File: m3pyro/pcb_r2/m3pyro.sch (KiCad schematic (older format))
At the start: 67 parts, among them IC1 STM32F405RxTx, IC2 TPS62130, IC3 MCP2562, IC4 TPS62150, J1 WEST TOP, J2 WEST BOT, J3 EAST TOP, J4 EAST BOT, Q1 Si5515CDC, Q2 Si5515CDC, Q3 Si5515CDC, Q4 Si5515CDC, Q5 Si5515CDC, Q6 Si5515CDC, Q7 Si5515CDC, Q8 Si5515CDC, Y1 26M

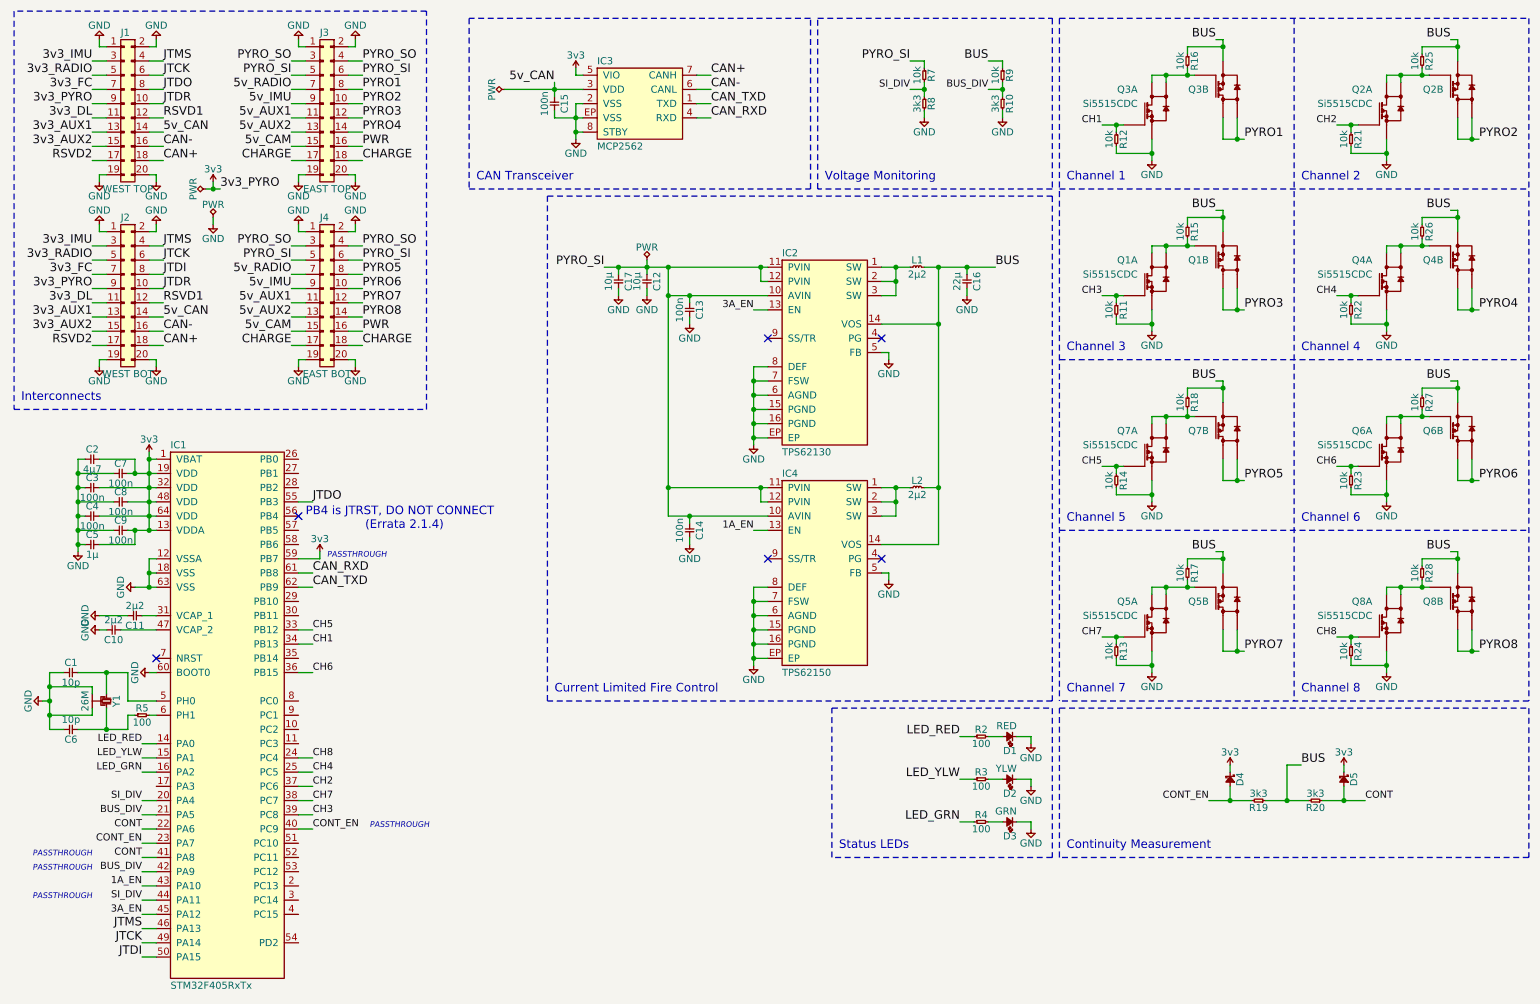
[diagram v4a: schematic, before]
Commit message: Update m3pyro so ch1-4 are bottom, 5-8 are top
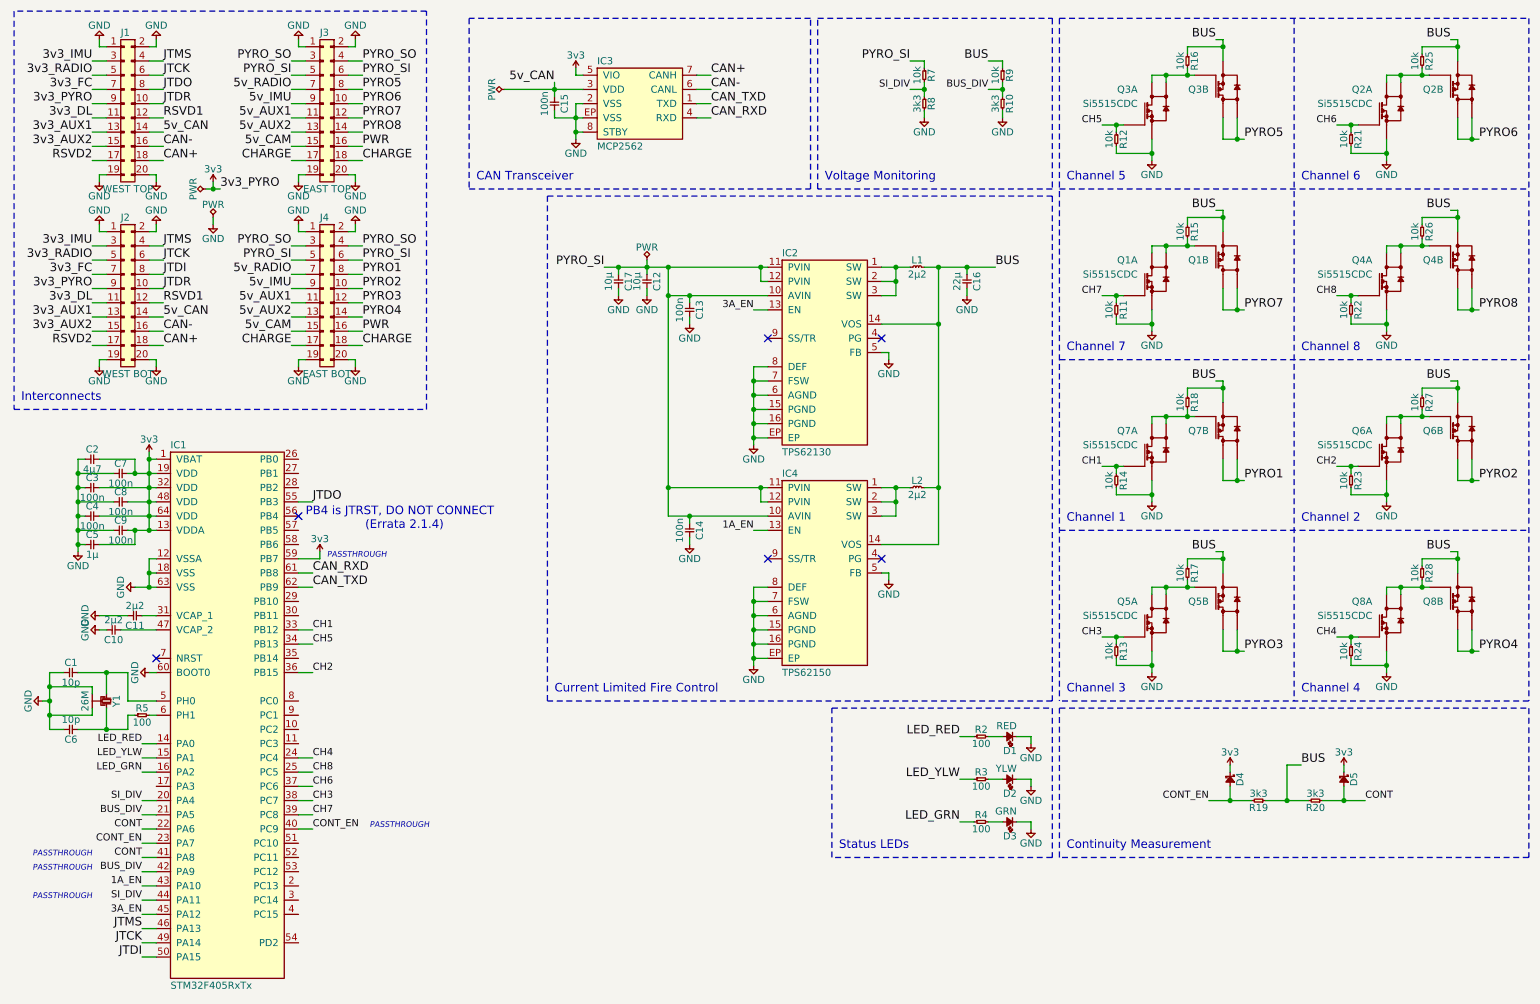
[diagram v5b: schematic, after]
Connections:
- net CH1: now also IC1.33 (PB12), Q7.2 (G1), R14.1; no longer IC1.34 (PB13), Q3.2 (G1), R12.1
- net CH2: now also IC1.36 (PB15), Q6.2 (G1), R23.1; no longer IC1.37 (PC6), Q2.2 (G1), R21.1
- net CH3: now also IC1.38 (PC7), Q5.2 (G1), R13.1; no longer IC1.39 (PC8), Q1.2 (G1), R11.1
- net CH4: now also IC1.24 (PC4), Q8.2 (G1), R24.1; no longer IC1.25 (PC5), Q4.2 (G1), R22.1
- net CH5: now also IC1.34 (PB13), Q3.2 (G1), R12.1; no longer IC1.33 (PB12), Q7.2 (G1), R14.1
- net CH6: now also IC1.37 (PC6), Q2.2 (G1), R21.1; no longer IC1.36 (PB15), Q6.2 (G1), R23.1
- net CH7: now also IC1.39 (PC8), Q1.2 (G1), R11.1; no longer IC1.38 (PC7), Q5.2 (G1), R13.1
- net CH8: now also IC1.25 (PC5), Q4.2 (G1), R22.1; no longer IC1.24 (PC4), Q8.2 (G1), R24.1
- net PYRO1: now also J4.8, Q7.5 (D2), Q7.6 (D2); no longer J3.8, Q3.5 (D2), Q3.6 (D2)
- net PYRO2: now also J4.10, Q6.5 (D2), Q6.6 (D2); no longer J3.10, Q2.5 (D2), Q2.6 (D2)
- net PYRO3: now also J4.12, Q5.5 (D2), Q5.6 (D2); no longer J3.12, Q1.5 (D2), Q1.6 (D2)
- net PYRO4: now also J4.14, Q8.5 (D2), Q8.6 (D2); no longer J3.14, Q4.5 (D2), Q4.6 (D2)
- net PYRO5: now also J3.8, Q3.5 (D2), Q3.6 (D2); no longer J4.8, Q7.5 (D2), Q7.6 (D2)
- net PYRO6: now also J3.10, Q2.5 (D2), Q2.6 (D2); no longer J4.10, Q6.5 (D2), Q6.6 (D2)
- net PYRO7: now also J3.12, Q1.5 (D2), Q1.6 (D2); no longer J4.12, Q5.5 (D2), Q5.6 (D2)
- net PYRO8: now also J3.14, Q4.5 (D2), Q4.6 (D2); no longer J4.14, Q8.5 (D2), Q8.6 (D2)
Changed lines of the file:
@@
 Text Label 2950 1450 0    60   ~ 0
 PWR
-Text Label 2950 1350 0    60   ~ 0
+Text Label 2950 2650 0    60   ~ 0
 PYRO4
-Text Label 2950 1250 0    60   ~ 0
+Text Label 2950 2550 0    60   ~ 0
 PYRO3
-Text Label 2950 1150 0    60   ~ 0
+Text Label 2950 2450 0    60   ~ 0
 PYRO2
-Text Label 2950 1050 0    60   ~ 0
+Text Label 2950 2350 0    60   ~ 0
 PYRO1
 $Comp
@@
 Text Label 2950 2750 0    60   ~ 0
 PWR
-Text Label 2950 2650 0    60   ~ 0
+Text Label 2950 1350 0    60   ~ 0
 PYRO8
-Text Label 2950 2550 0    60   ~ 0
+Text Label 2950 1250 0    60   ~ 0
 PYRO7
-Text Label 2950 2450 0    60   ~ 0
+Text Label 2950 1150 0    60   ~ 0
 PYRO6
-Text Label 2950 2350 0    60   ~ 0
+Text Label 2950 1050 0    60   ~ 0
 PYRO5
 Text Notes 550  3250 0    60   ~ 0
@@
 	2950 1450 2850 1450
 Wire Wire Line
+	2850 2650 2950 2650
+Wire Wire Line
+	2850 2550 2950 2550
+Wire Wire Line
+	2950 2450 2850 2450
+Wire Wire Line
+	2850 2350 2950 2350
+Wire Wire Line
+	2950 950  2850 950
+Wire Wire Line
+	2850 850  2950 850
+Wire Wire Line
+	2850 2050 2900 2050
+Wire Wire Line
+	2900 2050 2900 2000
+Wire Wire Line
+	2550 2050 2500 2050
+Wire Wire Line
+	2500 2050 2500 2000
+Wire Wire Line
+	2550 2950 2500 2950
+Wire Wire Line
+	2500 2950 2500 3000
+Wire Wire Line
+	2850 2950 2900 2950
+Wire Wire Line
+	2900 2950 2900 3000
+Wire Wire Line
+	2550 2150 2450 2150
+Wire Wire Line
+	2450 2250 2550 2250
+Wire Wire Line
+	2550 2350 2450 2350
+Wire Wire Line
+	2450 2450 2550 2450
+Wire Wire Line
+	2550 2550 2450 2550
+Wire Wire Line
+	2450 2650 2550 2650
+Wire Wire Line
+	2550 2750 2450 2750
+Wire Wire Line
+	2450 2850 2550 2850
+Wire Wire Line
+	2850 2850 2950 2850
+Wire Wire Line
+	2950 2750 2850 2750
+Wire Wire Line
 	2850 1350 2950 1350
 Wire Wire Line
@@
 Wire Wire Line
 	2850 1050 2950 1050
-Wire Wire Line
-	2950 950  2850 950
-Wire Wire Line
-	2850 850  2950 850
-Wire Wire Line
-	2850 2050 2900 2050
-Wire Wire Line
-	2900 2050 2900 2000
-Wire Wire Line
-	2550 2050 2500 2050
-Wire Wire Line
-	2500 2050 2500 2000
-Wire Wire Line
-	2550 2950 2500 2950
-Wire Wire Line
-	2500 2950 2500 3000
-Wire Wire Line
-	2850 2950 2900 2950
-Wire Wire Line
-	2900 2950 2900 3000
-Wire Wire Line
-	2550 2150 2450 2150
-Wire Wire Line
-	2450 2250 2550 2250
-Wire Wire Line
-	2550 2350 2450 2350
-Wire Wire Line
-	2450 2450 2550 2450
-Wire Wire Line
-	2550 2550 2450 2550
-Wire Wire Line
-	2450 2650 2550 2650
-Wire Wire Line
-	2550 2750 2450 2750
-Wire Wire Line
-	2450 2850 2550 2850
-Wire Wire Line
-	2850 2850 2950 2850
-Wire Wire Line
-	2950 2750 2850 2750
-Wire Wire Line
-	2850 2650 2950 2650
-Wire Wire Line
-	2850 2550 2950 2550
-Wire Wire Line
-	2950 2450 2850 2450
-Wire Wire Line
-	2850 2350 2950 2350
 Wire Wire Line
 	2950 2250 2850 2250
@@
 Connection ~ 8250 1300
 Text Label 8150 1300 2    50   ~ 0
-CH1
+CH5
 Wire Wire Line
 	8500 1000 8500 950
@@
 	9000 1400 9150 1400
 Text Label 9150 1400 0    60   ~ 0
-PYRO1
+PYRO5
 Wire Wire Line
 	8500 950  8800 950
@@
 	7850 550  7850 5350
 Text Notes 7900 1700 0    60   ~ 0
-Channel 1
+Channel 5
 Wire Notes Line
 	7850 550  11150 550
@@
 Connection ~ 9900 1300
 Text Label 9800 1300 2    50   ~ 0
-CH2
+CH6
 Wire Wire Line
 	10150 1000 10150 950
@@
 	10650 1400 10800 1400
 Text Label 10800 1400 0    60   ~ 0
-PYRO2
+PYRO6
 Wire Wire Line
 	10150 950  10450 950
@@
 	9500 550  9500 5350
 Text Notes 9550 1700 0    60   ~ 0
-Channel 2
+Channel 6
 $Comp
 L Si5515CDC Q1
@@
 Connection ~ 8250 2500
 Text Label 8150 2500 2    50   ~ 0
-CH3
+CH7
 Wire Wire Line
 	8500 2200 8500 2150
@@
 	9000 2600 9150 2600
 Text Label 9150 2600 0    60   ~ 0
-PYRO3
+PYRO7
 Wire Wire Line
 	8500 2150 8800 2150
@@
 Connection ~ 9100 2600
 Text Notes 7900 2900 0    60   ~ 0
-Channel 3
+Channel 7
 Wire Notes Line
 	7850 1750 11150 1750
@@
 Connection ~ 9900 2500
 Text Label 9800 2500 2    50   ~ 0
-CH4
+CH8
 Wire Wire Line
 	10150 2200 10150 2150
@@
 	10650 2600 10800 2600
 Text Label 10800 2600 0    60   ~ 0
-PYRO4
+PYRO8
 Wire Wire Line
 	10150 2150 10450 2150
@@
 Connection ~ 10750 2600
 Text Notes 9550 2900 0    60   ~ 0
-Channel 4
+Channel 8
 $Comp
 L Si5515CDC Q7
@@
 Connection ~ 8250 3700
 Text Label 8150 3700 2    50   ~ 0
-CH5
+CH1
 Wire Wire Line
 	8500 3400 8500 3350
@@
 	9000 3800 9150 3800
 Text Label 9150 3800 0    60   ~ 0
-PYRO5
+PYRO1
 Wire Wire Line
 	8500 3350 8800 3350
@@
 Connection ~ 9100 3800
 Text Notes 7900 4100 0    60   ~ 0
-Channel 5
+Channel 1
 Wire Notes Line
 	7850 2950 11150 2950
@@
 Connection ~ 9900 3700
 Text Label 9800 3700 2    50   ~ 0
-CH6
+CH2
 Wire Wire Line
 	10150 3400 10150 3350
@@
 	10650 3800 10800 3800
 Text Label 10800 3800 0    60   ~ 0
-PYRO6
+PYRO2
 Wire Wire Line
 	10150 3350 10450 3350
@@
 Connection ~ 10750 3800
 Text Notes 9550 4100 0    60   ~ 0
-Channel 6
+Channel 2
 $Comp
 L Si5515CDC Q5
@@
 Connection ~ 8250 4900
 Text Label 8150 4900 2    50   ~ 0
-CH7
+CH3
 Wire Wire Line
 	8500 4600 8500 4550
@@
 	9000 5000 9150 5000
 Text Label 9150 5000 0    60   ~ 0
-PYRO7
+PYRO3
 Wire Wire Line
 	8500 4550 8800 4550
@@
 Connection ~ 9100 5000
 Text Notes 7900 5300 0    60   ~ 0
-Channel 7
+Channel 3
 Wire Notes Line
 	7850 4150 11150 4150
@@
 Connection ~ 9900 4900
 Text Label 9800 4900 2    50   ~ 0
-CH8
+CH4
 Wire Wire Line
 	10150 4600 10150 4550
@@
 	10650 5000 10800 5000
 Text Label 10800 5000 0    60   ~ 0
-PYRO8
+PYRO4
 Wire Wire Line
 	10150 4550 10450 4550
@@
 Connection ~ 10750 5000
 Text Notes 9550 5300 0    60   ~ 0
-Channel 8
+Channel 4
 Wire Notes Line
 	11150 5350 7850 5350
@@
 Voltage Monitoring
 Text Label 2600 4950 0    50   ~ 0
+CH5
+Text Label 2600 5950 0    50   ~ 0
+CH6
+Text Label 2600 6150 0    50   ~ 0
+CH7
+Text Label 2600 5850 0    50   ~ 0
+CH8
+Text Label 2600 4850 0    50   ~ 0
 CH1
-Text Label 2600 5950 0    50   ~ 0
+Text Label 2600 5150 0    50   ~ 0
 CH2
-Text Label 2600 6150 0    50   ~ 0
+Text Label 2600 6050 0    50   ~ 0
 CH3
-Text Label 2600 5850 0    50   ~ 0
+Text Label 2600 5750 0    50   ~ 0
 CH4
-Text Label 2600 4850 0    50   ~ 0
-CH5
-Text Label 2600 5150 0    50   ~ 0
-CH6
-Text Label 2600 6050 0    50   ~ 0
-CH7
-Text Label 2600 5750 0    50   ~ 0
-CH8
 Wire Notes Line
 	7800 1800 7800 5350

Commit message: m3pyro r2 bom
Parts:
- added X1: BACKUP 22µ, symbol PART
- C12, C17: Farnell (none) -> 2211164
- C13, C14: Farnell (none) -> 2496771
- C16: Farnell (none) -> 2494232
- R10, R19, R20, R8: Farnell (none) -> 2447170
- R11, R12, R13, R14, R15, R16, R17, R18, R21, R22, R23, R24, R25, R26, R27, R28, R7, R9: Farnell (none) -> 2379805
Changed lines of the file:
@@
 F 2 "agg:0603" H 7200 2350 50  0001 C CNN
 F 3 "" H 7200 2350 50  0001 C CNN
+F 4 "2494232" H 7200 2350 60  0001 C CNN "Farnell"
 	1    7200 2350
 	0    1    1    0
@@
 F 2 "agg:0603" H 4950 2350 50  0001 C CNN
 F 3 "" H 4950 2350 50  0001 C CNN
+F 4 "2211164" H 0   0   60  0001 C CNN "Farnell"
 	1    4950 2350
 	0    1    1    0
@@
 F 2 "agg:0402" H 5250 2550 50  0001 C CNN
 F 3 "" H 5250 2550 50  0001 C CNN
+F 4 "2496771" H 0   0   60  0001 C CNN "Farnell"
 	1    5250 2550
 	0    1    1    0
@@
 F 2 "agg:0402" H 5250 4100 50  0001 C CNN
 F 3 "" H 5250 4100 50  0001 C CNN
+F 4 "2496771" H 0   0   60  0001 C CNN "Farnell"
 	1    5250 4100
 	0    1    1    0
@@
 F 2 "agg:0402" H 6900 900 50  0001 C CNN
 F 3 "" H 6900 900 50  0001 C CNN
+F 4 "2379805" H 0   0   60  0001 C CNN "Farnell"
 	1    6900 900
 	0    1    1    0
@@
 F 2 "agg:0402" H 6900 1100 50  0001 C CNN
 F 3 "" H 6900 1100 50  0001 C CNN
+F 4 "2447170" H 0   0   60  0001 C CNN "Farnell"
 	1    6900 1100
 	0    1    1    0
@@
 F 2 "agg:0402" H 9300 6050 50  0001 C CNN
 F 3 "" H 9300 6050 50  0001 C CNN
+F 4 "2447170" H 0   0   60  0001 C CNN "Farnell"
 	1    9300 6050
 	-1   0    0    1
@@
 F 2 "agg:0402" H 9700 6050 50  0001 C CNN
 F 3 "" H 9700 6050 50  0001 C CNN
+F 4 "2447170" H 0   0   60  0001 C CNN "Farnell"
 	1    9700 6050
 	-1   0    0    1
@@
 F 2 "agg:0402" H 7450 900 50  0001 C CNN
 F 3 "" H 7450 900 50  0001 C CNN
+F 4 "2379805" H 0   0   60  0001 C CNN "Farnell"
 	1    7450 900
 	0    1    1    0
@@
 F 2 "agg:0402" H 7450 1100 50  0001 C CNN
 F 3 "" H 7450 1100 50  0001 C CNN
+F 4 "2447170" H 0   0   60  0001 C CNN "Farnell"
 	1    7450 1100
 	0    1    1    0
@@
 F 2 "agg:0402" H 8250 1350 50  0001 C CNN
 F 3 "" H 8250 1350 50  0001 C CNN
+F 4 "2379805" H 0   0   60  0001 C CNN "Farnell"
 	1    8250 1350
 	0    1    1    0
@@
 F 2 "agg:0402" H 8750 800 50  0001 C CNN
 F 3 "" H 8750 800 50  0001 C CNN
+F 4 "2379805" H 0   0   60  0001 C CNN "Farnell"
 	1    8750 800
 	0    1    1    0
@@
 F 2 "agg:0402" H 9900 1350 50  0001 C CNN
 F 3 "" H 9900 1350 50  0001 C CNN
+F 4 "2379805" H 0   0   60  0001 C CNN "Farnell"
 	1    9900 1350
 	0    1    1    0
@@
 F 2 "agg:0402" H 10400 800 50  0001 C CNN
 F 3 "" H 10400 800 50  0001 C CNN
+F 4 "2379805" H 0   0   60  0001 C CNN "Farnell"
 	1    10400 800
 	0    1    1    0
@@
 F 2 "agg:0402" H 8250 2550 50  0001 C CNN
 F 3 "" H 8250 2550 50  0001 C CNN
+F 4 "2379805" H 0   0   60  0001 C CNN "Farnell"
 	1    8250 2550
 	0    1    1    0
@@
 F 2 "agg:0402" H 8750 2000 50  0001 C CNN
 F 3 "" H 8750 2000 50  0001 C CNN
+F 4 "2379805" H 0   0   60  0001 C CNN "Farnell"
 	1    8750 2000
 	0    1    1    0
@@
 F 2 "agg:0402" H 9900 2550 50  0001 C CNN
 F 3 "" H 9900 2550 50  0001 C CNN
+F 4 "2379805" H 0   0   60  0001 C CNN "Farnell"
 	1    9900 2550
 	0    1    1    0
@@
 F 2 "agg:0402" H 10400 2000 50  0001 C CNN
 F 3 "" H 10400 2000 50  0001 C CNN
+F 4 "2379805" H 0   0   60  0001 C CNN "Farnell"
 	1    10400 2000
 	0    1    1    0
@@
 F 2 "agg:0402" H 8250 3750 50  0001 C CNN
 F 3 "" H 8250 3750 50  0001 C CNN
+F 4 "2379805" H 0   0   60  0001 C CNN "Farnell"
 	1    8250 3750
 	0    1    1    0
@@
 F 2 "agg:0402" H 8750 3200 50  0001 C CNN
 F 3 "" H 8750 3200 50  0001 C CNN
+F 4 "2379805" H 0   0   60  0001 C CNN "Farnell"
 	1    8750 3200
 	0    1    1    0
@@
 F 2 "agg:0402" H 9900 3750 50  0001 C CNN
 F 3 "" H 9900 3750 50  0001 C CNN
+F 4 "2379805" H 0   0   60  0001 C CNN "Farnell"
 	1    9900 3750
 	0    1    1    0
@@
 F 2 "agg:0402" H 10400 3200 50  0001 C CNN
 F 3 "" H 10400 3200 50  0001 C CNN
+F 4 "2379805" H 0   0   60  0001 C CNN "Farnell"
 	1    10400 3200
 	0    1    1    0
@@
 F 2 "agg:0402" H 8250 4950 50  0001 C CNN
 F 3 "" H 8250 4950 50  0001 C CNN
+F 4 "2379805" H 0   0   60  0001 C CNN "Farnell"
 	1    8250 4950
 	0    1    1    0
@@
 F 2 "agg:0402" H 8750 4400 50  0001 C CNN
 F 3 "" H 8750 4400 50  0001 C CNN
+F 4 "2379805" H 0   0   60  0001 C CNN "Farnell"
 	1    8750 4400
 	0    1    1    0
@@
 F 2 "agg:0402" H 9900 4950 50  0001 C CNN
 F 3 "" H 9900 4950 50  0001 C CNN
+F 4 "2379805" H 0   0   60  0001 C CNN "Farnell"
 	1    9900 4950
 	0    1    1    0
@@
 F 2 "agg:0402" H 10400 4400 50  0001 C CNN
 F 3 "" H 10400 4400 50  0001 C CNN
+F 4 "2379805" H 0   0   60  0001 C CNN "Farnell"
 	1    10400 4400
 	0    1    1    0
@@
 F 2 "agg:0603" H 4750 2350 50  0001 C CNN
 F 3 "" H 4750 2350 50  0001 C CNN
+F 4 "2211164" H 0   0   60  0001 C CNN "Farnell"
 	1    4750 2350
 	0    1    1    0
@@
 Wire Wire Line
 	4750 2500 4750 2450
+$Comp
+L PART X1
+U 1 1 5989FF85
+P 7200 3000
+F 0 "X1" H 7250 3100 50  0000 L CNN
+F 1 "BACKUP 22µ" H 7250 3000 50  0000 L CNN
+F 2 "" H 7200 3000 50  0001 C CNN
+F 3 "" H 7200 3000 50  0001 C CNN
+F 4 "2346921" H 7200 3000 60  0001 C CNN "Farnell"
+	1    7200 3000
+	1    0    0    -1
+$EndComp
 $EndSCHEMATC
